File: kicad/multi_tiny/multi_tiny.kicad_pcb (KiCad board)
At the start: 2 copper layers, 105.4 x 88.9 mm, 69 parts, among them J1 Conn_02x03_Odd_Even, J2 Conn_01x08, J3 28pin ZIF, J4 Conn_01x17, SW1 SW_SPDT, SW2 SW_SPDT, SW4 SW_SPST, SW5 SW_SPST, U1 CD4052B, U2 CD4052B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

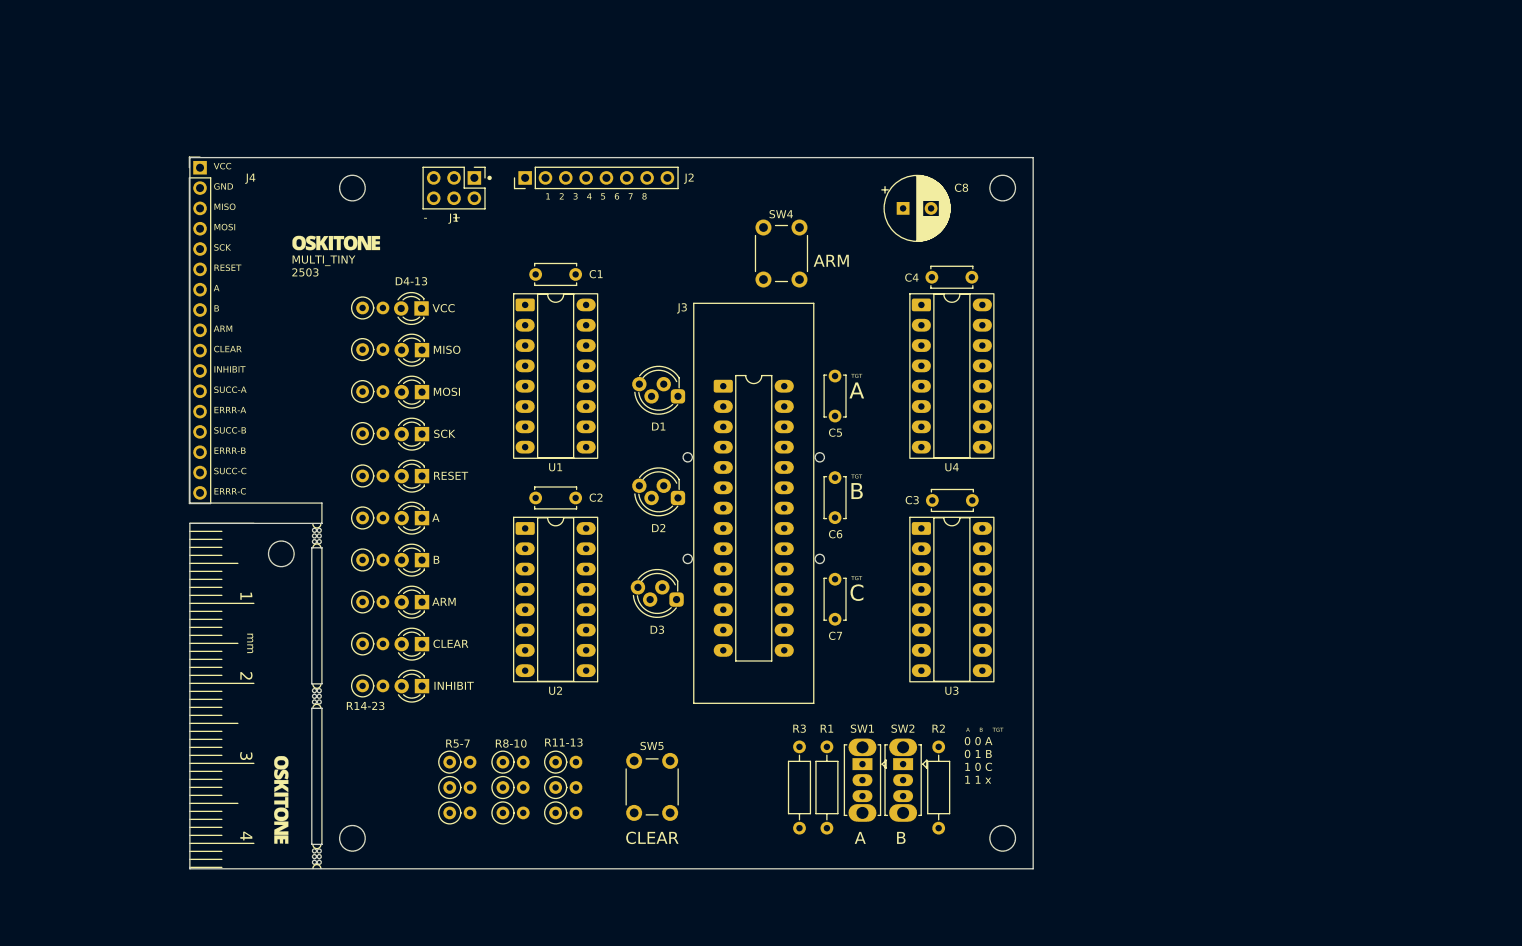
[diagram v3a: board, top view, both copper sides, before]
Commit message: Route PCB
And fix CD4052/target pins arrangement
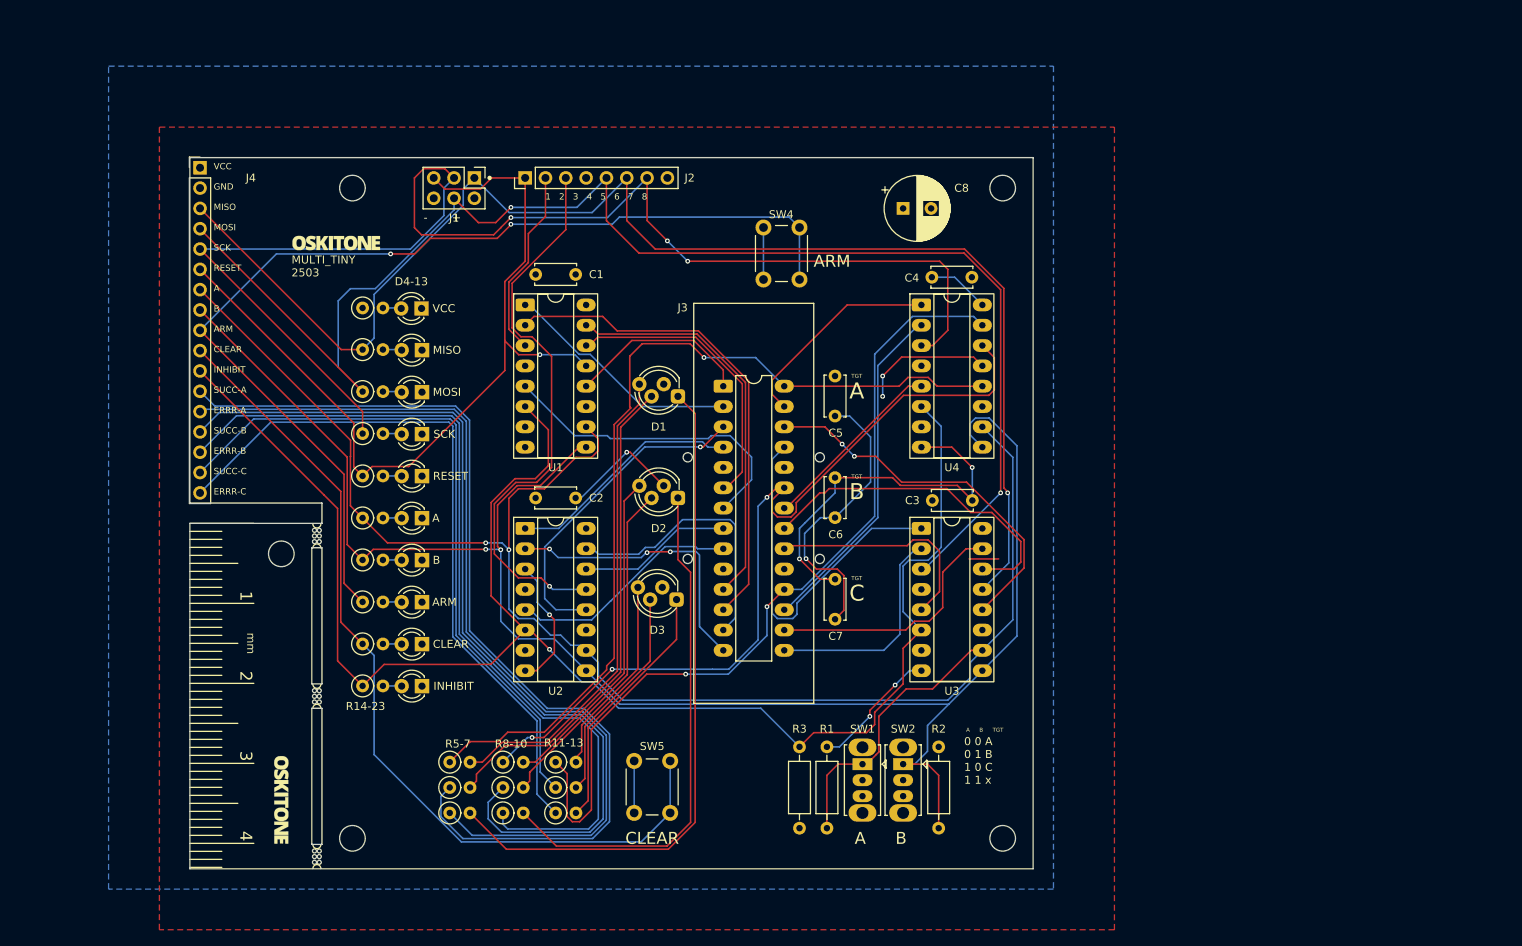
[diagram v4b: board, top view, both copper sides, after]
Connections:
- U2 pad 1: 6-A -> 4-A
- U2 pad 12: 5-A -> 3-A
- U2 pad 13: 5 -> 3
- U2 pad 14: 5-B -> 3-B
- U2 pad 15: 5-C -> 3-C
- U2 pad 2: 6-C -> 4-C
- U2 pad 3: 6 -> 4
- U2 pad 5: 6-B -> 4-B
- U3 pad 1: 3-A -> 5-A
- U3 pad 12: 4-A -> 6-A
- U3 pad 13: 4 -> 6
- U3 pad 14: 4-B -> 6-B
- U3 pad 15: 4-C -> 6-C
- U3 pad 2: 3-C -> 5-C
- U3 pad 3: 3 -> 5
- U3 pad 5: 3-B -> 5-B
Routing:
- net A: track 0.00 -> 222.8 mm, vias 0 -> 2
- net B: track 0.00 -> 215.9 mm, vias 0 -> 2
- net INHIBIT: track 0.00 -> 204.8 mm, vias 0 -> 1
- net 5: track 0.00 -> 182.1 mm, vias 0 -> 2
- net 6: track 0.00 -> 172.7 mm, vias 0 -> 1
- net 7: track 0.00 -> 170.6 mm, vias 0 -> 3
- net ARM: track 0.00 -> 130.2 mm, vias 0 -> 2
- net SUCCESS-A: track 0.00 -> 122.5 mm
- net ERROR-A: track 0.00 -> 115.4 mm
- net SUCCESS-B: track 0.00 -> 114.3 mm
- net 8-A: track 0.00 -> 112.7 mm, vias 0 -> 2
- net CLEAR: track 0.00 -> 109.0 mm
- net ERROR-B: track 0.00 -> 108.1 mm
- net 1: track 0.00 -> 106.7 mm, vias 0 -> 1
- net 8-C: track 0.00 -> 106.1 mm, vias 0 -> 2
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- added copper zone on B.Cu, net 4
- added copper zone on F.Cu, net 8

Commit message: Obviate/ignore DRC warnings
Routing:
- net 8: track 78.4 -> 116.5 mm, vias 3 -> 4
- net INHIBIT: track 204.8 -> 211.4 mm
- net CLEAR: track 109.0 -> 115.3 mm
- net 6: track 172.7 -> 178.6 mm
- net 7: track 170.6 -> 176.3 mm
- net ARM: track 130.2 -> 135.4 mm
- net 5: track 182.1 -> 187.2 mm
- net A: track 222.8 -> 227.7 mm
- net B: track 215.9 -> 220.3 mm
- net 1: track 106.7 -> 110.8 mm
- net ERROR-C: track 89.1 -> 92.6 mm
- net 3: track 70.4 -> 73.6 mm
- net 1-A: track 23.1 -> 25.4 mm
- net SUCCESS-C: track 85.6 -> 87.9 mm
- net 4: track 95.2 -> 93.3 mm
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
